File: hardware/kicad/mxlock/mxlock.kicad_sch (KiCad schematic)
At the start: 21 parts, among them J1 ATMEL-ICE-10, J2 Conn_01x06, J3 Conn_01x02, J4 Conn_01x02, J5 Conn_01x02, Q1 2N3904, SW1 SW_SL, SW2 SW_CAPS, SW3 SW_4080, U1 CD4066BM, U2 ATtiny214/414/814

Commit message: Use "mxlock" for project files
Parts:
- J1: footprint stevekey:PinHeader_2x05_P1.27mm_Shrouded_Vertical_SMD_Handsolder -> mxlock:PinHeader_2x05_P1.27mm_Shrouded_Vertical_SMD_Handsolder; symbol stevekey:ATMEL-ICE-10 -> mxlock:ATMEL-ICE-10
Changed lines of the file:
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@@
     (pin "1")
     (instances
-      (project "stevekey"
+      (project "mxlock"
         (path "/4393a5c5-44f8-4de9-9c92-ea247f2f7df2"
           (reference "#PWR011") (unit 1)
@@
     (pin "7")
     (instances
-      (project "stevekey"
+      (project "mxlock"
         (path "/4393a5c5-44f8-4de9-9c92-ea247f2f7df2"
           (reference "U1") (unit 1)
@@
     (pin "1")
     (instances
-      (project "stevekey"
+      (project "mxlock"
         (path "/4393a5c5-44f8-4de9-9c92-ea247f2f7df2"
           (reference "#PWR04") (unit 1)
@@
     (pin "1")
     (instances
-      (project "stevekey"
+      (project "mxlock"
         (path "/4393a5c5-44f8-4de9-9c92-ea247f2f7df2"
           (reference "#PWR013") (unit 1)
@@
     (pin "2")
     (instances
-      (project "stevekey"
+      (project "mxlock"
         (path "/4393a5c5-44f8-4de9-9c92-ea247f2f7df2"
           (reference "D2") (unit 1)
@@
     (pin "1")
     (instances
-      (project "stevekey"
+      (project "mxlock"
         (path "/4393a5c5-44f8-4de9-9c92-ea247f2f7df2"
           (reference "#PWR08") (unit 1)
@@
     (pin "1")
     (instances
-      (project "stevekey"
+      (project "mxlock"
         (path "/4393a5c5-44f8-4de9-9c92-ea247f2f7df2"
           (reference "#PWR02") (unit 1)
@@
     (pin "2")
     (instances
-      (project "stevekey"
+      (project "mxlock"
         (path "/4393a5c5-44f8-4de9-9c92-ea247f2f7df2"
           (reference "R7") (unit 1)
@@
     (pin "7")
     (instances
-      (project "stevekey"
+      (project "mxlock"
         (path "/4393a5c5-44f8-4de9-9c92-ea247f2f7df2"
           (reference "U1") (unit 3)
@@
     (pin "9")
     (instances
-      (project "stevekey"
+      (project "mxlock"
         (path "/4393a5c5-44f8-4de9-9c92-ea247f2f7df2"
           (reference "U2") (unit 1)
@@
     (pin "2")
     (instances
-      (project "stevekey"
+      (project "mxlock"
         (path "/4393a5c5-44f8-4de9-9c92-ea247f2f7df2"
           (reference "R6") (unit 1)
@@
     (pin "2")
     (instances
-      (project "stevekey"
+      (project "mxlock"
         (path "/4393a5c5-44f8-4de9-9c92-ea247f2f7df2"
           (reference "C3") (unit 1)
@@
     (pin "1")
     (instances
-      (project "stevekey"
+      (project "mxlock"
         (path "/4393a5c5-44f8-4de9-9c92-ea247f2f7df2"
           (reference "#PWR09") (unit 1)
@@
     (pin "1")
     (instances
-      (project "stevekey"
+      (project "mxlock"
         (path "/4393a5c5-44f8-4de9-9c92-ea247f2f7df2"
           (reference "#PWR05") (unit 1)
@@
     (pin "2")
     (instances
-      (project "stevekey"
+      (project "mxlock"
         (path "/4393a5c5-44f8-4de9-9c92-ea247f2f7df2"
           (reference "SW3") (unit 1)
@@
     (pin "7")
     (instances
-      (project "stevekey"
+      (project "mxlock"
         (path "/4393a5c5-44f8-4de9-9c92-ea247f2f7df2"
           (reference "U1") (unit 2)
@@
     (pin "2")
     (instances
-      (project "stevekey"
+      (project "mxlock"
         (path "/4393a5c5-44f8-4de9-9c92-ea247f2f7df2"
           (reference "SW2") (unit 1)
@@
     )
   )
-  (symbol (lib_id "stevekey:ATMEL-ICE-10") (at 190.5 44.45 0) (unit 1)
+  (symbol (lib_id "mxlock:ATMEL-ICE-10") (at 190.5 44.45 0) (unit 1)
     (in_bom yes) (on_board yes) (dnp no)
     (property "Reference" "J1" (at 210.82 26.67 0)
@@
       (effects (font (size 1.27 1.27)) (justify right))
     )
-    (property "Footprint" "stevekey:PinHeader_2x05_P1.27mm_Shrouded_Vertical_SMD_Handsolder" (at 186.69 40.64 90)
+    (property "Footprint" "mxlock:PinHeader_2x05_P1.27mm_Shrouded_Vertical_SMD_Handsolder" (at 186.69 40.64 90)
       (effects (font (size 1.27 1.27)) hide)
     )
@@
     (pin "9")
     (instances
-      (project "stevekey"
+      (project "mxlock"
         (path "/4393a5c5-44f8-4de9-9c92-ea247f2f7df2"
           (reference "J1") (unit 1)
@@
     (pin "1")
     (instances
-      (project "stevekey"
+      (project "mxlock"
         (path "/4393a5c5-44f8-4de9-9c92-ea247f2f7df2"
           (reference "#PWR012") (unit 1)
@@
     (pin "1")
     (instances
-      (project "stevekey"
+      (project "mxlock"
         (path "/4393a5c5-44f8-4de9-9c92-ea247f2f7df2"
           (reference "#PWR06") (unit 1)
@@
     (pin "1")
     (instances
-      (project "stevekey"
+      (project "mxlock"
         (path "/4393a5c5-44f8-4de9-9c92-ea247f2f7df2"
           (reference "#PWR03") (unit 1)
@@
     (pin "3")
     (instances
-      (project "stevekey"
+      (project "mxlock"
         (path "/4393a5c5-44f8-4de9-9c92-ea247f2f7df2"
           (reference "Q1") (unit 1)
@@
     (pin "2")
     (instances
-      (project "stevekey"
+      (project "mxlock"
         (path "/4393a5c5-44f8-4de9-9c92-ea247f2f7df2"
           (reference "C2") (unit 1)
@@
     (pin "2")
     (instances
-      (project "stevekey"
+      (project "mxlock"
         (path "/4393a5c5-44f8-4de9-9c92-ea247f2f7df2"
           (reference "D1") (unit 1)
@@
     (pin "2")
     (instances
-      (project "stevekey"
+      (project "mxlock"
         (path "/4393a5c5-44f8-4de9-9c92-ea247f2f7df2"
           (reference "C1") (unit 1)
@@
     (pin "1")
     (instances
-      (project "stevekey"
+      (project "mxlock"
         (path "/4393a5c5-44f8-4de9-9c92-ea247f2f7df2"
           (reference "#PWR01") (unit 1)
@@
     (pin "2")
     (instances
-      (project "stevekey"
+      (project "mxlock"
         (path "/4393a5c5-44f8-4de9-9c92-ea247f2f7df2"
           (reference "R4") (unit 1)
@@
     (pin "2")
     (instances
-      (project "stevekey"
+      (project "mxlock"
         (path "/4393a5c5-44f8-4de9-9c92-ea247f2f7df2"
           (reference "R5") (unit 1)
@@
     (pin "2")
     (instances
-      (project "stevekey"
+      (project "mxlock"
         (path "/4393a5c5-44f8-4de9-9c92-ea247f2f7df2"
           (reference "J4") (unit 1)
@@
     (pin "2")
     (instances
-      (project "stevekey"
+      (project "mxlock"
         (path "/4393a5c5-44f8-4de9-9c92-ea247f2f7df2"
           (reference "SW1") (unit 1)
@@
     (pin "2")
     (instances
-      (project "stevekey"
+      (project "mxlock"
         (path "/4393a5c5-44f8-4de9-9c92-ea247f2f7df2"
           (reference "J3") (unit 1)
@@
     (pin "6")
     (instances
-      (project "stevekey"
+      (project "mxlock"
         (path "/4393a5c5-44f8-4de9-9c92-ea247f2f7df2"
           (reference "J2") (unit 1)
@@
     (pin "2")
     (instances
-      (project "stevekey"
+      (project "mxlock"
         (path "/4393a5c5-44f8-4de9-9c92-ea247f2f7df2"
           (reference "D3") (unit 1)
@@
     (pin "2")
     (instances
-      (project "stevekey"
+      (project "mxlock"
         (path "/4393a5c5-44f8-4de9-9c92-ea247f2f7df2"
           (reference "J5") (unit 1)
@@
     (pin "7")
     (instances
-      (project "stevekey"
+      (project "mxlock"
         (path "/4393a5c5-44f8-4de9-9c92-ea247f2f7df2"
           (reference "U1") (unit 5)
@@
     (pin "7")
     (instances
-      (project "stevekey"
+      (project "mxlock"
         (path "/4393a5c5-44f8-4de9-9c92-ea247f2f7df2"
           (reference "U1") (unit 4)
@@
     (pin "1")
     (instances
-      (project "stevekey"
+      (project "mxlock"
         (path "/4393a5c5-44f8-4de9-9c92-ea247f2f7df2"
           (reference "#PWR07") (unit 1)
@@
     (pin "1")
     (instances
-      (project "stevekey"
+      (project "mxlock"
         (path "/4393a5c5-44f8-4de9-9c92-ea247f2f7df2"
           (reference "#PWR010") (unit 1)

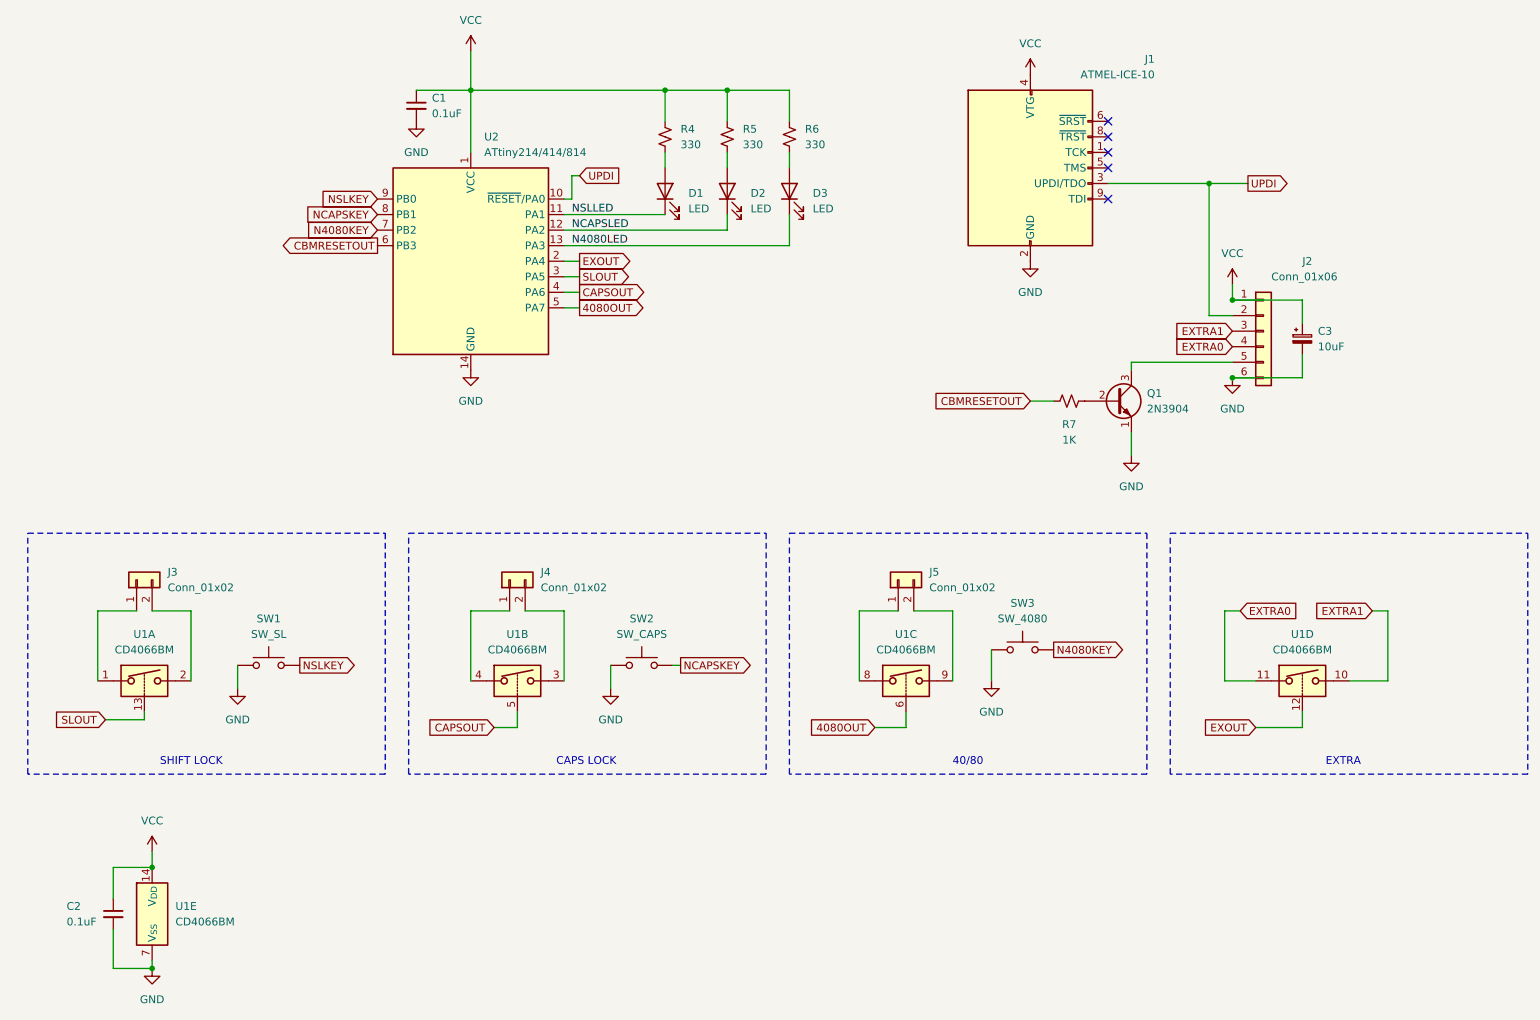
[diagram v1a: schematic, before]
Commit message: Add fourth key to the schematic
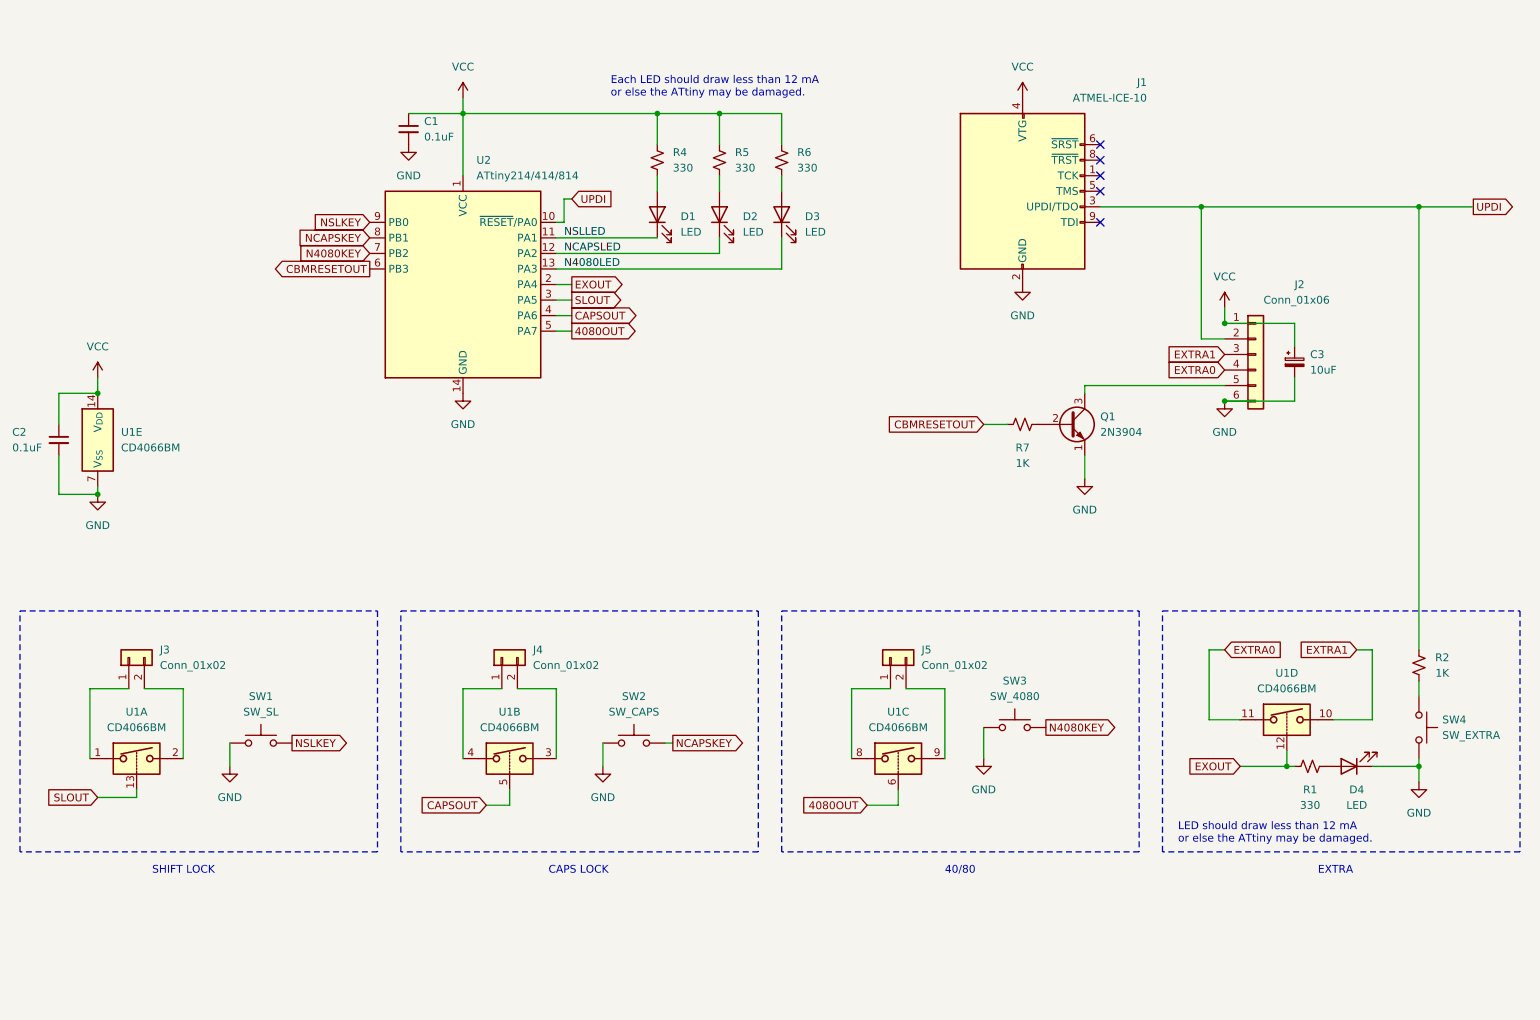
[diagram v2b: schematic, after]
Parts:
- added D4: LED, LED_THT:LED_D5.0mm, symbol Device:LED
- added R1: 330, Resistor_THT:R_Axial_DIN0204_L3.6mm_D1.6mm_P7.62mm_Horizontal, symbol Device:R_Small_US
- added R2: 1K, Resistor_THT:R_Axial_DIN0204_L3.6mm_D1.6mm_P7.62mm_Horizontal, symbol Device:R_Small_US
- added SW4: SW_EXTRA, Button_Switch_Keyboard:SW_Cherry_MX_1.00u_PCB, symbol Switch:SW_Push
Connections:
- net EXOUT: now also R1.1
- net GND: now also D4.1 (K), SW4.2
- net UPDI: now also R2.2
- new net: R2.1, SW4.1
- new net: D4.2 (A), R1.2
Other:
- note added: "Each LED should draw less than 12 mA or else the ATtiny may be damaged."
- note added: "LED should draw less than 12 mA or else the ATtiny may be damaged."
- moved on the sheet: C1, C2, C3, D1, D2, D3, J1, J2, J3, J4, J5, Q1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

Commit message: Add fourth key to the PCB layout
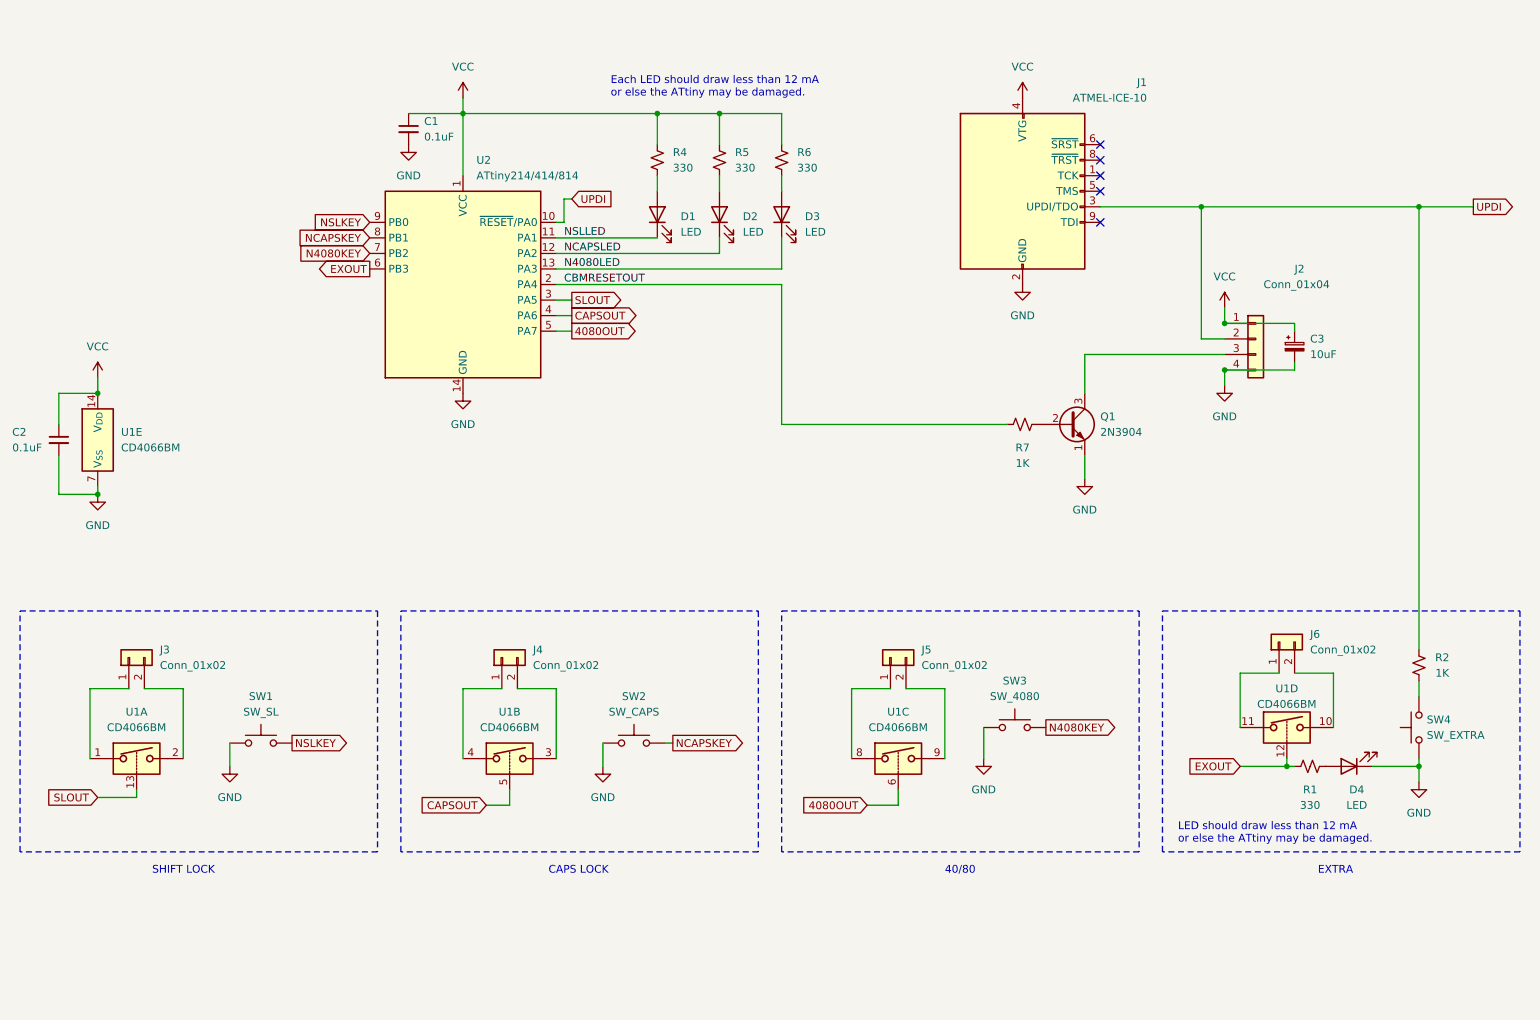
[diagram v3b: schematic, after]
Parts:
- removed J2: Conn_01x06, Connector_PinHeader_2.54mm:PinHeader_1x06_P2.54mm_Vertical, symbol Connector_Generic:Conn_01x06
- added J2: Conn_01x04, Connector_PinHeader_2.54mm:PinHeader_1x04_P2.54mm_Vertical, symbol Connector_Generic:Conn_01x04
- added J6: Conn_01x02, Connector_PinHeader_2.54mm:PinHeader_1x02_P2.54mm_Vertical, symbol Connector_Generic:Conn_01x02
- Q1: footprint Package_TO_SOT_THT:TO-92_Inline -> Package_TO_SOT_THT:TO-92_HandSolder
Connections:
- net CBMRESETOUT: now also U2.2 (PA4); no longer U2.6 (PB3)
- net EXOUT: now also U2.6 (PB3); no longer U2.2 (PA4)
- net GND: now also SW4.1, J2.4 (Pin_4); no longer SW4.2
- net UPDI: now also J2.2 (Pin_2)
- net VCC: now also J2.1 (Pin_1)
- net at R2.1: now also SW4.2; no longer SW4.1
- net at Q1.3 (C): now also J2.3 (Pin_3)
- net EXTRA0: no longer names the net of U1.11
- net EXTRA0: now also J6.1 (Pin_1)
- net EXTRA1: no longer names the net of U1.10
- net EXTRA1: now also J6.2 (Pin_2)
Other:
- moved on the sheet: C3, SW4, U1D

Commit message: Use consistent reference designators
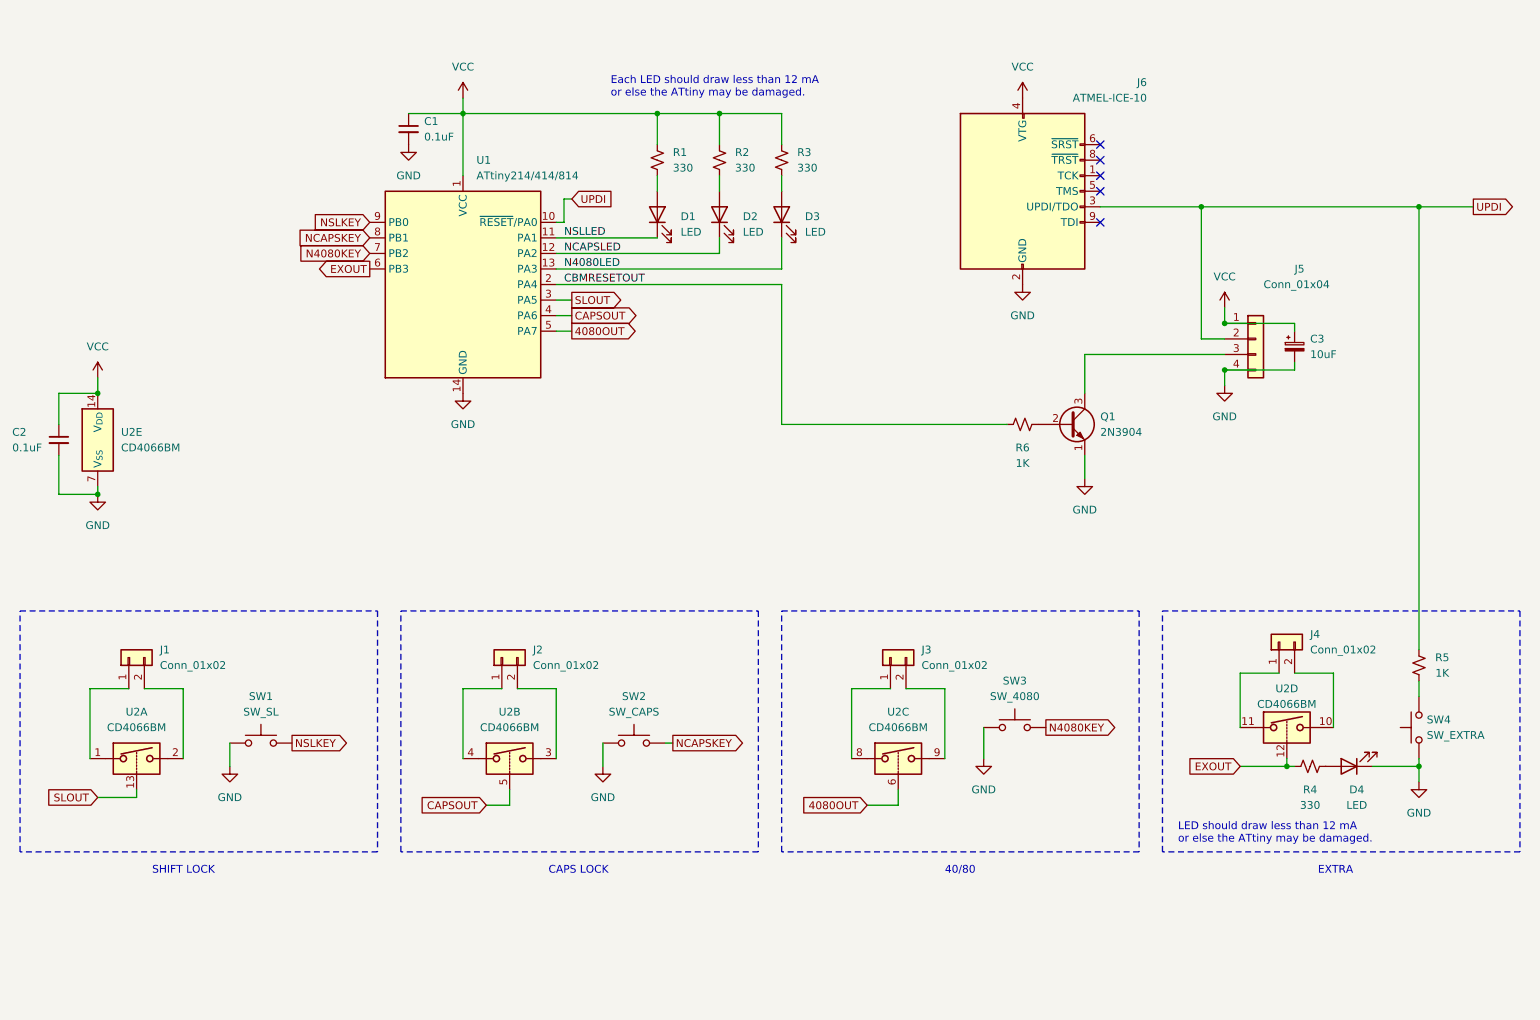
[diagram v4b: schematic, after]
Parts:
- renumbered J3 to J1, J4 to J2, J5 to J3, J6 to J4, J2 to J5, J1 to J6, R4 to R1, R5 to R2, R6 to R3, R1 to R4, R2 to R5, R7 to R6, U2 to U1, U1 to U2
